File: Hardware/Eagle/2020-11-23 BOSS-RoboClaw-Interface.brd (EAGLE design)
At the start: 41.5 x 48.3 mm, 8 parts, among them IC1 ISO7221A, J2 PINHD-1X2-MOLEX-22112022, J3 Molex 22122034, X1 Amphenol L77SDAH15SOL2RM8C309

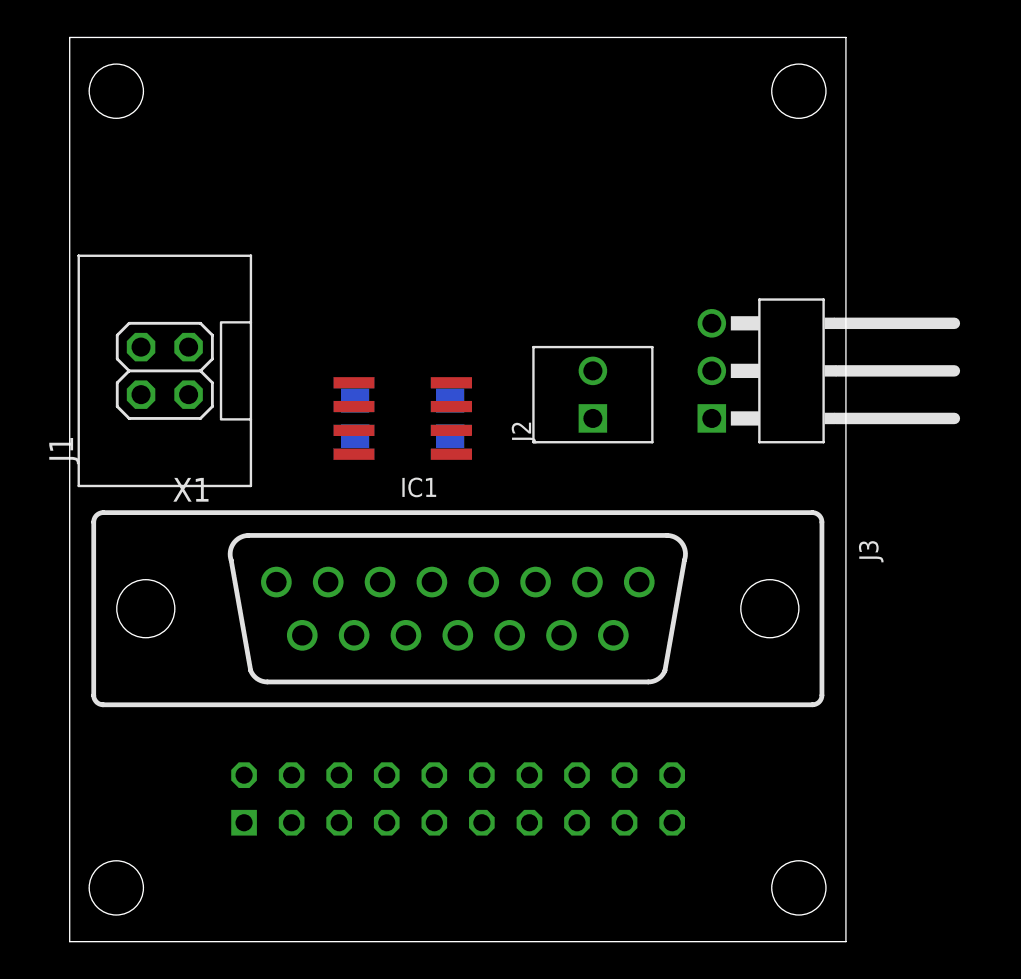
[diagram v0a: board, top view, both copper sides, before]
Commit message: Created schematic PDF and saved 2020-11-23 version
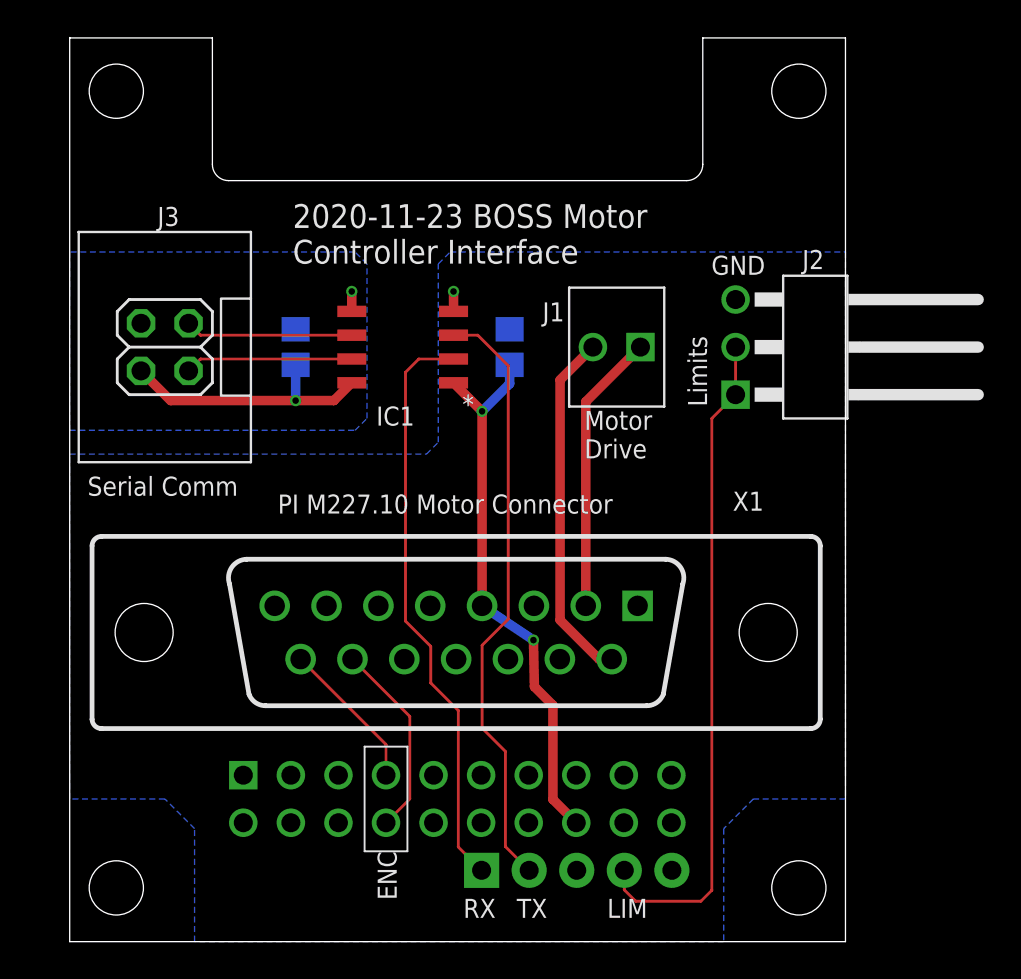
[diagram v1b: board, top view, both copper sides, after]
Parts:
- removed J4: (no value), AUmlib:FE10-2-SAMTEC-ESW-110-44-S-D
- added J5: SAMTEC ESQ-110-33-T-D, AUmlib:2X10-ESQ-110-33-T-D
- added J6: SAMTEC-ESQ-105-33-T-S, AUmlib:1X05-ESQ-105-33-T-S
- IC1: value ISO7221A -> TI ISO7221ADR; device AUmlib:SO-08 -> AUmlib:SO-08-ISO7221
- J1: value (none) -> MOLEX 22112022; device AUmlib:2X02-SHROUD -> AUmlib:1X02-MOLEX-22112022
- J2: value PINHD-1X2-MOLEX-22112022 -> MOLEX 22122034; device AUmlib:1X02-MOLEX-22112022 -> AUmlib:1X03RA-MOLEX-22122034
- J3: value Molex 22122034 -> Amphenol 75869-130LF; device AUmlib:1X03RA-MOLEX-22122034 -> AUmlib:2X02-SHROUD
- moved J3 33.0 mm to (5.08, 31.8)
- moved J1 24.2 mm to (29.2, 31.8), turned to 180 degrees
- moved J2 12.0 mm to (39.4, 31.8)
- moved C1 4.96 mm to (23.5, 31.8)
- moved C2 4.96 mm to (12.1, 31.8)
- moved IC1 3.81 mm to (17.8, 31.8), turned to 180 degrees
- moved X1 1.27 mm to (20.6, 16.5)
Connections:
- removed net LIMIT/HOME: J3.1, J3.2
- removed net N$1: IC1.7, J1.1
- removed net N$2: IC1.6, J1.3
- new net LIMIT: J2.1, J2.2, J6.4
- new net RXMCU: IC1.6, J3.3
- new net TXMCU: IC1.7, J3.1
- net ENC1A: now also J5.8
- net ENC1B: now also J5.7
- net GND: now also J2.3, J5.15; no longer J3.3
- net GND-ISO: now also J3.4; no longer J1.4
- net M1A: now also J1.1, X1.2; no longer J2.2, X1.9
- net M1B: now also J1.2, X1.9; no longer J2.1, X1.2
- net RX: now also J6.1
- net TX: now also J6.2
- net VCC1: now also J5.16
- net VCC2: now also J3.2; no longer J1.2
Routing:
- net LIMIT: track 0.00 -> 35.7 mm
- net TX: track 0.00 -> 32.2 mm
- net RX: track 0.00 -> 31.1 mm
- net VCC1: track 0.00 -> 29.6 mm, vias 0 -> 2
- net M1B: track 0.00 -> 18.9 mm
- net M1A: track 0.00 -> 15.0 mm
- net VCC2: track 0.00 -> 14.2 mm, vias 0 -> 1
- net ENC1A: track 0.00 -> 10.5 mm
- net RXMCU: track 0.00 -> 8.98 mm
- net TXMCU: track 0.00 -> 8.98 mm
- net ENC1B: track 0.00 -> 8.09 mm
- net GND-ISO: track 0.00 -> 1.07 mm, vias 0 -> 1
- net GND: track 0.00 -> 1.07 mm, vias 0 -> 1
- added copper zone on layer 16, net GND
- added copper zone on layer 16, net GND-ISO
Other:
- board size 41.5 x 48.3 mm -> 41.4 x 48.3 mm
- board text added: "2020-11-23 BOSS Motor Controller Interface"
- board text added: "ENC"
- board text added: "GND"
- board text added: "LIM"
- board text added: "Limits"
- board text added: "Motor Drive"
- board text added: "PI DB-15 Motor Connector Edge"
- board text added: "PI M227.10 Motor Connector"
- board text added: "RX"
- board text added: "Serial Comm"
- board text added: "TX"
- board text removed: "2019-03-01 BOSS Spectrograph PI M-227.10 Motor to Basic Micro RoboClaw2x7A Controller"
